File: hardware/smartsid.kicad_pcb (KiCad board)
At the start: 2 copper layers, 39.4 x 56.4 mm, 35 parts, among them P1 INPUT, P2 CONTROL, P3 POT2, P4 SOCKET, P5 OUTPUT, U1 GAL16V8, U2 SID2, U3 7812, U4 7809, U5 SID1

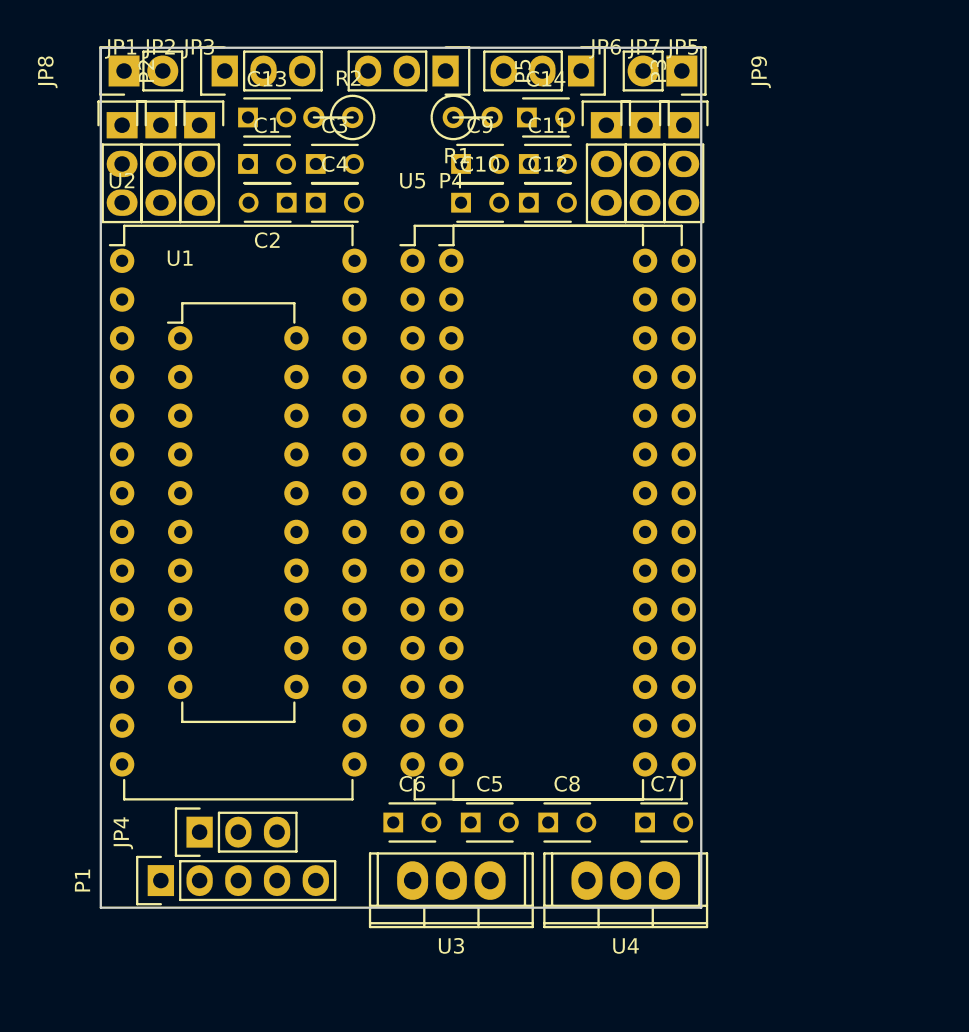
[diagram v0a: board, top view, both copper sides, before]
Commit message: Hardware: Added mixing and simple opamp output circuit
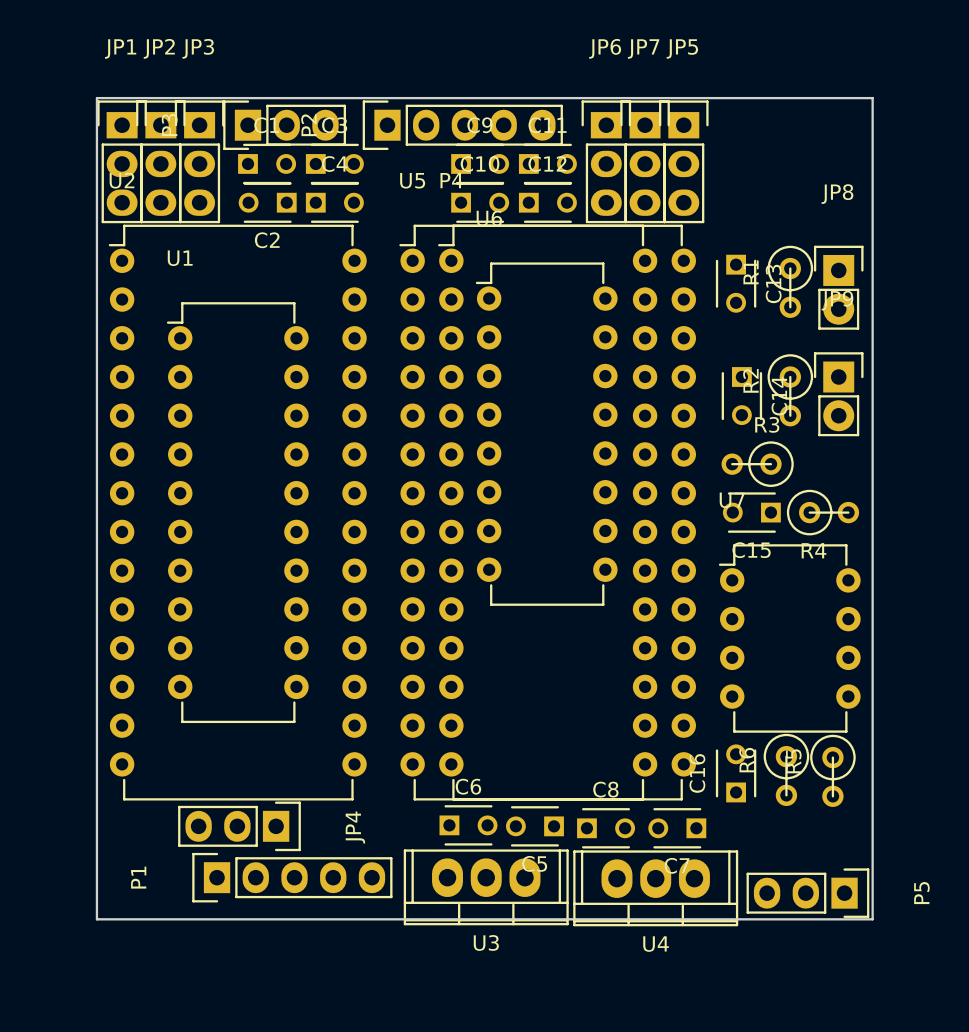
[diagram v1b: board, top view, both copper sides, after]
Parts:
- added C15: 2.2u, Capacitors_ThroughHole:C_Disc_D3_P2.5, F.Cu at (174.0, 96.5)
- added C16: 2.2u, Capacitors_ThroughHole:C_Disc_D3_P2.5, F.Cu at (171.7, 114.9)
- added R3: 1k, Discret:R1, F.Cu at (172.7, 93.3)
- added R4: 47k, Discret:R1, F.Cu at (177.8, 96.5)
- added R5: 1k, Discret:R1, F.Cu at (178.1, 113.9)
- added R6: 47k, Discret:R1, F.Cu at (175.0, 113.8)
- added U6: 4052, Housings_DIP:DIP-16_W7.62mm, F.Cu at (155.5, 82.5)
- added U7: TL072, Housings_DIP:DIP-8_W7.62mm, F.Cu at (171.4, 101.0)
- P2: footprint Pin_Headers:Pin_Header_Straight_1x03 -> Pin_Headers:Pin_Header_Straight_1x05
- moved P5 59.9 mm to (178.8, 121.5)
- moved JP8 48.7 mm to (178.4, 80.6), turned to 0 degrees
- moved R2 35.1 mm to (175.3, 88.9), turned to 270 degrees
- moved C13 33.4 mm to (171.7, 80.3), turned to 270 degrees
- moved R1 23.6 mm to (175.3, 81.8), turned to 270 degrees
- moved JP9 22.5 mm to (178.4, 87.6), turned to 0 degrees
- moved P3 22.1 mm to (139.7, 71.1), turned to 90 degrees
- moved C14 22.1 mm to (172.1, 87.6), turned to 270 degrees
- moved P2 11.2 mm to (148.8, 71.1)
- moved C5 5.47 mm to (159.8, 117.1), turned to 180 degrees
- moved JP4 5.03 mm to (141.5, 117.1), turned to 270 degrees
- moved C6 3.69 mm to (152.9, 117.0)
- moved P1 3.69 mm to (137.7, 120.5)
- moved C7 3.39 mm to (169.1, 117.2), turned to 180 degrees
- moved C8 2.57 mm to (161.9, 117.2)
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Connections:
- C7 pad 1: /+12V -> VDD
- JP1 pad 1: /+12V -> VDD
- JP4 pad 2: /+12V -> VDD
- JP5 pad 1: /+12V -> VDD
- P5 pad 1: /S1OUT -> GND
- P5 pad 2: GND -> /RIGHT
- P5 pad 3: /S2OUT -> /LEFT
- U4 pad 1: /+12V -> VDD
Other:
- board size 39.4 x 56.4 mm -> 50.9 x 53.8 mm

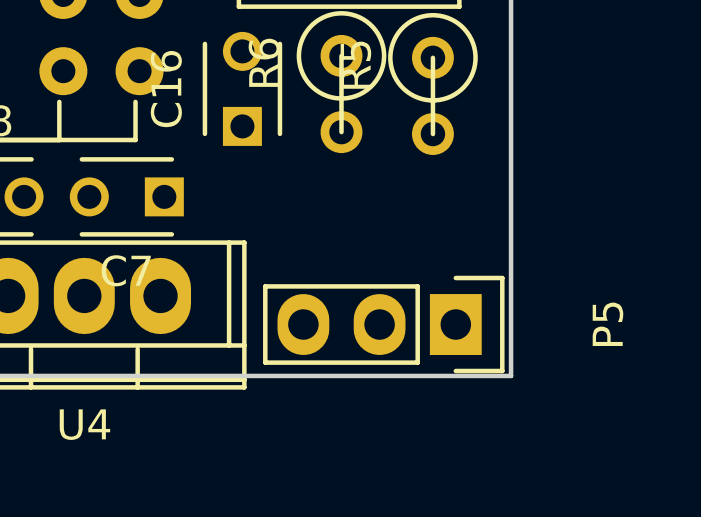
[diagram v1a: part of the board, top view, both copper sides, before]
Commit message: Hardware: Added notes about where to get +16v on 250469
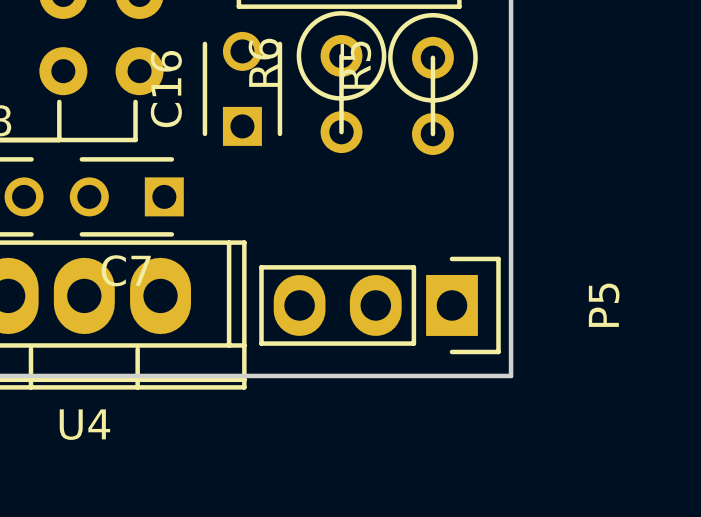
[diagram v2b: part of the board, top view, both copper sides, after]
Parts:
- moved P5 0.65 mm to (178.7, 120.8)
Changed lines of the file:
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@@
   )
   (module Pin_Headers:Pin_Header_Straight_1x03 (layer F.Cu)
-    (at 178.816 121.4755 270)
+    (at 178.689 120.8405 270)
     (descr "Through hole pin header")
     (tags "pin header")

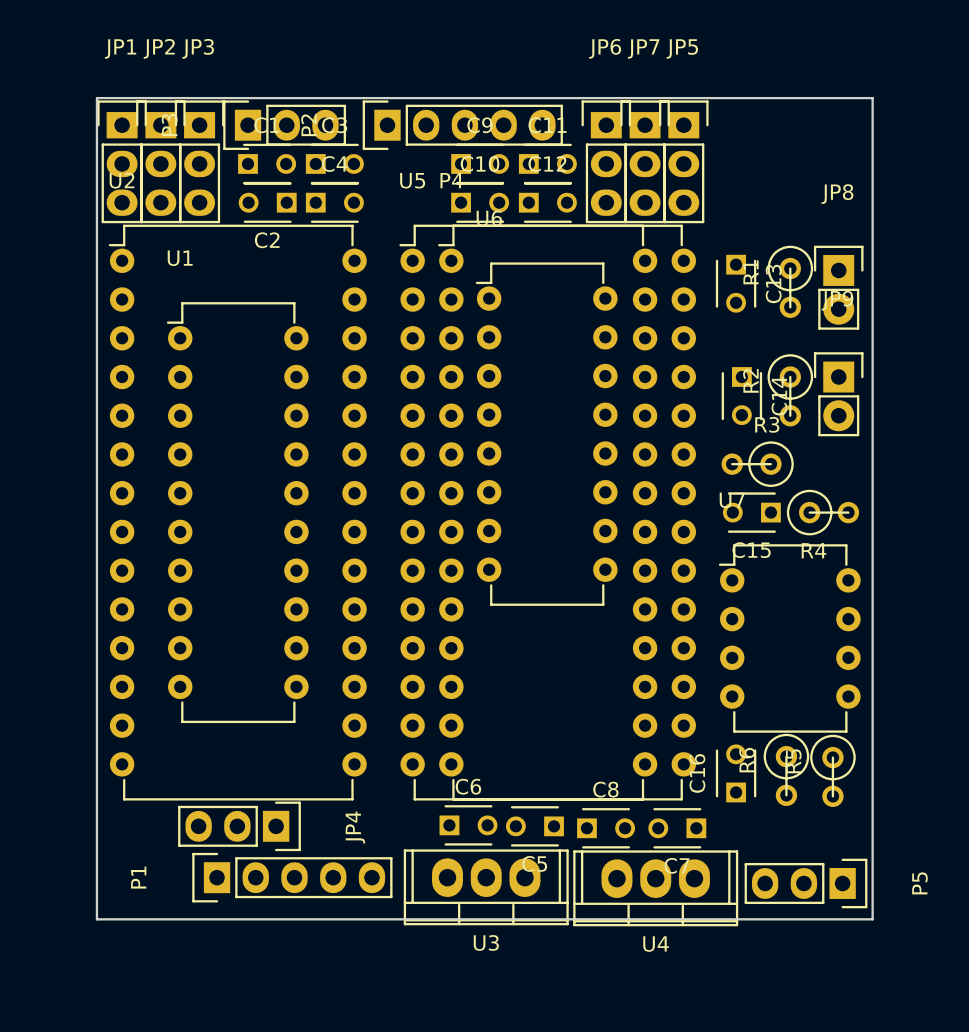
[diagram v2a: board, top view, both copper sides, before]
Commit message: Hardware: Added optional digifix circuits for both chips
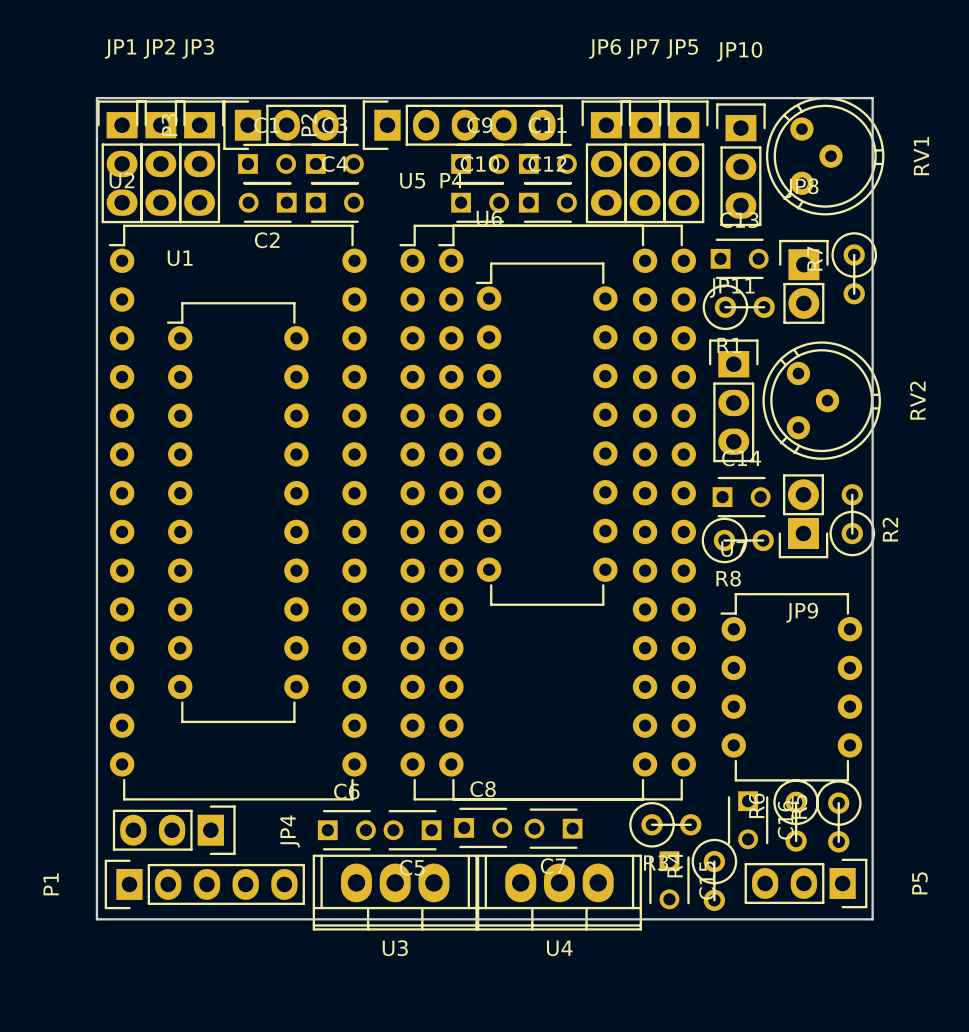
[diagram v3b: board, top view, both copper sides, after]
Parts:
- added JP10: DIGIFIX2, Pin_Headers:Pin_Header_Straight_1x03, F.Cu at (172.0, 71.3)
- added JP11: DIGIFIX1, Pin_Headers:Pin_Header_Straight_1x03, F.Cu at (171.6, 86.8)
- added R7: 220k, Discret:R1, F.Cu at (179.5, 80.9)
- added R8: 220k, Discret:R1, F.Cu at (172.2, 98.3)
- added RV1: 1M, Potentiometers:Potentiometer_Bourns_3339H_Angular_ScrewUp, F.Cu at (176.0, 71.4)
- added RV2: 1M, Potentiometers:Potentiometer_Bourns_3339H_Angular_ScrewUp, F.Cu at (175.8, 87.4)
- moved R4 25.3 mm to (170.3, 120.7), turned to 270 degrees
- moved R3 24.2 mm to (167.5, 117.0), turned to 0 degrees
- moved C15 23.8 mm to (167.3, 119.4), turned to 270 degrees
- moved JP9 10.5 mm to (176.1, 97.9), turned to 180 degrees
- moved R2 8.73 mm to (179.3, 96.6), turned to 90 degrees
- moved C7 8.12 mm to (161.0, 117.2)
- moved C8 8.05 mm to (153.9, 117.2)
- moved C5 8.03 mm to (151.7, 117.3)
- moved C6 7.98 mm to (144.9, 117.3)
- moved C14 7.98 mm to (170.8, 95.5), turned to 0 degrees
- moved U4 6.32 mm to (160.1, 120.8)
- moved U3 5.98 mm to (149.4, 120.8)
- moved P1 5.76 mm to (131.9, 120.9)
- moved JP4 4.29 mm to (137.3, 117.3)
- moved R1 3.24 mm to (172.3, 83.1), turned to 0 degrees
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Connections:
- net /+9VUNREG renamed /+16V
- U2 pad 26: Net-(C13-Pad2) -> Net-(JP10-Pad1)
- U5 pad 26: Net-(C14-Pad2) -> Net-(JP11-Pad1)

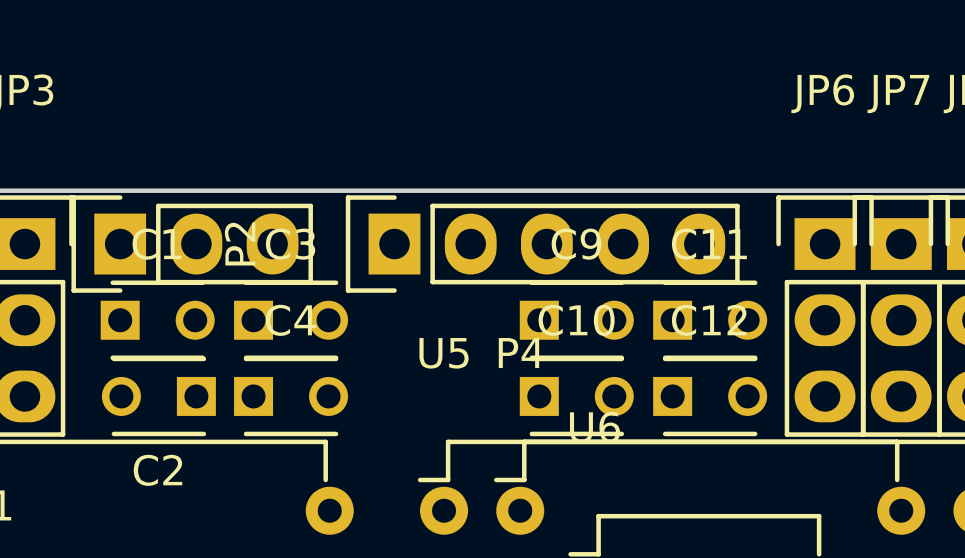
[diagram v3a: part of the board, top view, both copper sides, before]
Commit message: Hardware/Firmware: Supply separate IO enable lines (IO1EN, IO2EN)
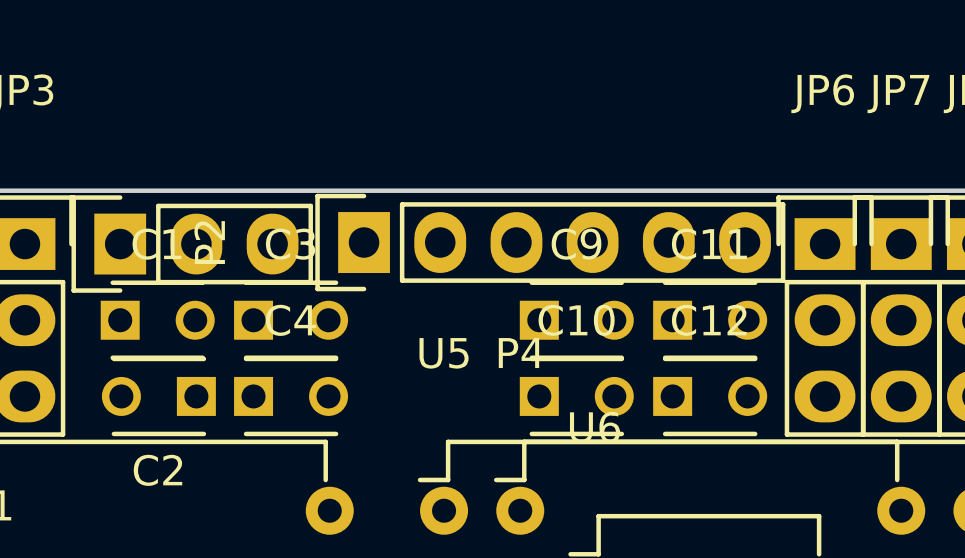
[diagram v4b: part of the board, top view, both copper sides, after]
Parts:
- P2: footprint Pin_Headers:Pin_Header_Straight_1x05 -> Pin_Headers:Pin_Header_Straight_1x06
- moved P2 1.02 mm to (147.8, 71.1)
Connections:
- net /IO renamed /IO1EN
- P2 pad 4: /M0 -> /IO2EN
- P2 pad 5: /M1 -> /M0
- U1 pad 19: Net-(U1-Pad19) -> /IO2EN

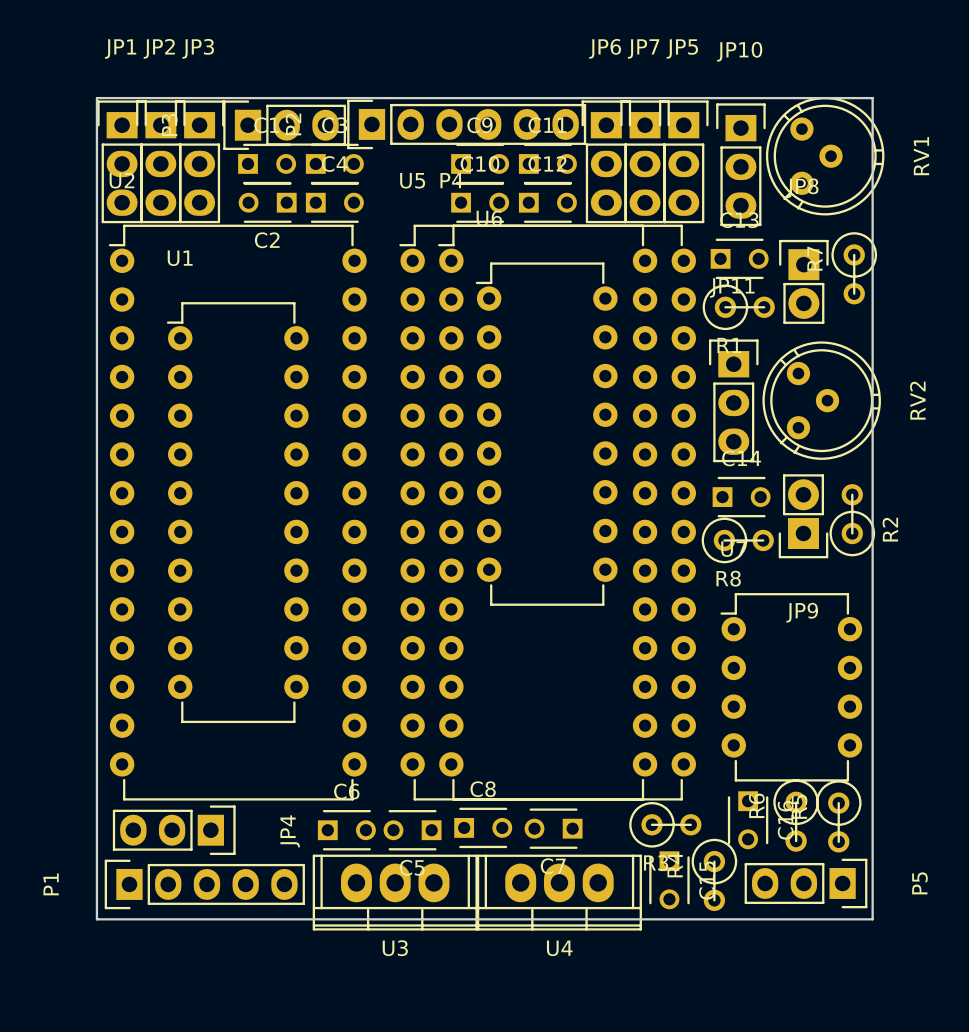
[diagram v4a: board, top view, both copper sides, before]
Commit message: Hardware: Removed digifix circuits, added 7660, mix after opamps
The 4052 can only mix signals within 2-8V and VCC must be <10V. Therefore
the amplified output must be mixed.
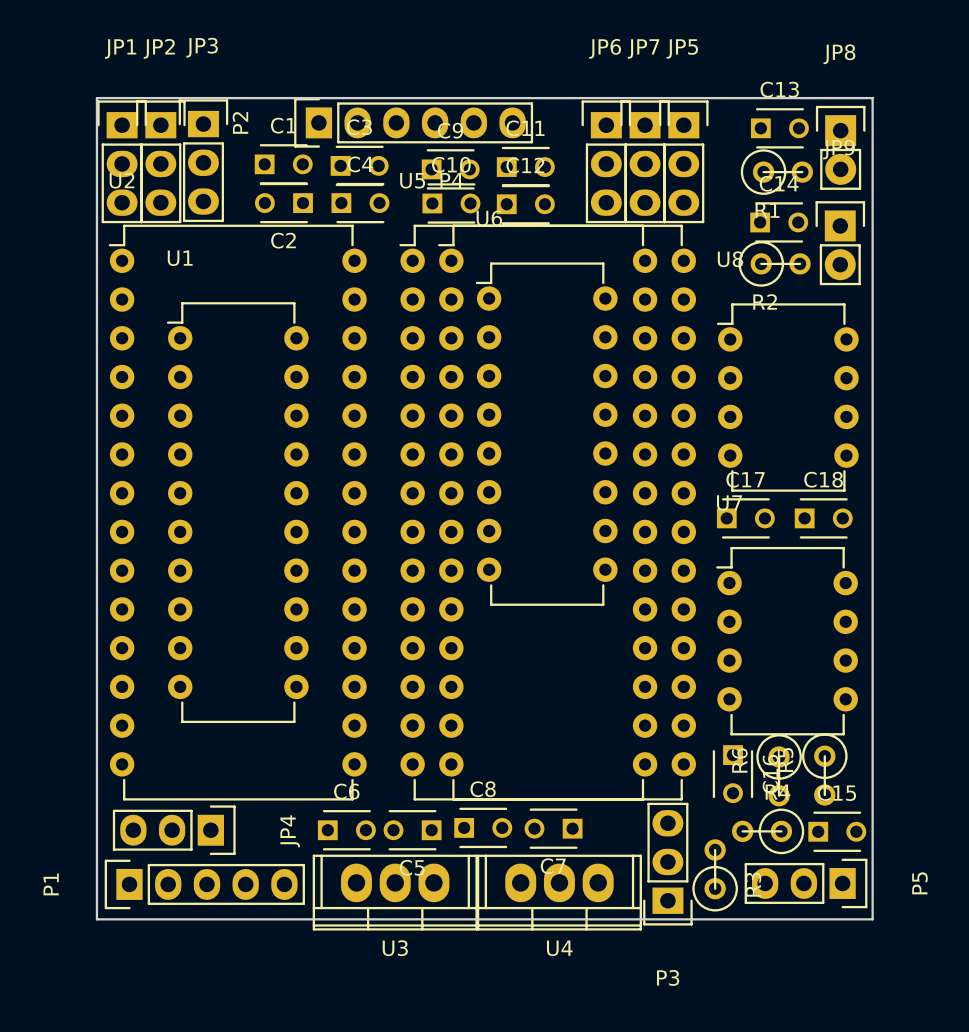
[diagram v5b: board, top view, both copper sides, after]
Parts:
- removed JP10: DIGIFIX2, Pin_Headers:Pin_Header_Straight_1x03
- removed JP11: DIGIFIX1, Pin_Headers:Pin_Header_Straight_1x03
- removed R7, R8: 220k, Discret:R1
- removed RV1, RV2: 1M, Potentiometers:Potentiometer_Bourns_3339H_Angular_ScrewUp
- added C17: 10u, Capacitors_ThroughHole:C_Disc_D3_P2.5, F.Cu at (171.1, 96.9)
- added C18: 10u, Capacitors_ThroughHole:C_Disc_D3_P2.5, F.Cu at (176.2, 96.9)
- added U8: ICL7660, Housings_DIP:DIP-8_W7.62mm, F.Cu at (171.3, 85.2)
- moved P3 57.8 mm to (167.2, 122.0), turned to 180 degrees
- moved JP9 20.3 mm to (178.5, 77.7), turned to 0 degrees
- moved C14 18.2 mm to (173.3, 77.5)
- moved R2 17.1 mm to (174.6, 80.2), turned to 0 degrees
- moved C15 9.94 mm to (177.1, 117.5), turned to 0 degrees
- moved R1 9.21 mm to (174.8, 74.2)
- moved JP8 9.11 mm to (178.6, 71.5)
- moved C13 8.96 mm to (173.3, 71.3)
- moved R4 4.51 mm to (173.4, 117.4), turned to 180 degrees
- moved R3 4.09 mm to (170.3, 119.9), turned to 90 degrees
- moved P2 3.48 mm to (144.3, 71.0)
- moved R5 3.21 mm to (177.5, 113.8)
- moved C16 3.18 mm to (171.5, 112.4)
- moved R6 3.18 mm to (174.5, 113.8)
- moved U7 3.04 mm to (171.3, 101.1)
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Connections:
- net Net-(C6-Pad1) renamed /PWR
- C7 pad 1: VDD -> /+12V
- JP1 pad 1: VDD -> /+12V
- JP4 pad 2: VDD -> /+12V
- JP5 pad 1: VDD -> /+12V
- P5 pad 2: /RIGHT -> /RIGHT_OUT
- P5 pad 3: /LEFT -> /LEFT_OUT
- R3 pad 2: /LEFT_MIXED -> /S1OUT
- R5 pad 2: /RIGHT_MIXED -> /S2OUT
- U2 pad 26: Net-(JP10-Pad1) -> Net-(C13-Pad2)
- U4 pad 1: VDD -> /+12V
- U5 pad 26: Net-(JP11-Pad1) -> Net-(C14-Pad2)
- U6 pad 1: /S1OUT -> /LEFT
- U6 pad 11: /S2OUT -> /RIGHT
- U6 pad 12: /S1OUT -> /LEFT
- U6 pad 13: /LEFT_MIXED -> /LEFT_OUT
- U6 pad 14: /S2OUT -> /RIGHT
- U6 pad 15: /S1OUT -> /LEFT
- U6 pad 2: /S2OUT -> /RIGHT
- U6 pad 3: /RIGHT_MIXED -> /RIGHT_OUT
- U6 pad 4: /S1OUT -> /LEFT
- U6 pad 5: /S2OUT -> /RIGHT
- U6 pad 7: GND -> /VEE
- U7 pad 8: VDD -> /+12V
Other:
- net class Power added: clearance 0.2, trace_width 0.5, via_dia 0.6, via_drill 0.4
